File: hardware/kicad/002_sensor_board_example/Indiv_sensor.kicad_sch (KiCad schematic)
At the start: 5 parts, among them Q301 AO3400A, U301 VCNT2025X01

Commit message: Main Controller Board (1D) now added. Cheaper design, with RP2354, and BUCK PMIC
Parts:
- renumbered Q301 to Q4301, R301 to R4301, R302 to R4302, R303 to R4303, U301 to U4301
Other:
- company: (none) -> Noah Jaffe

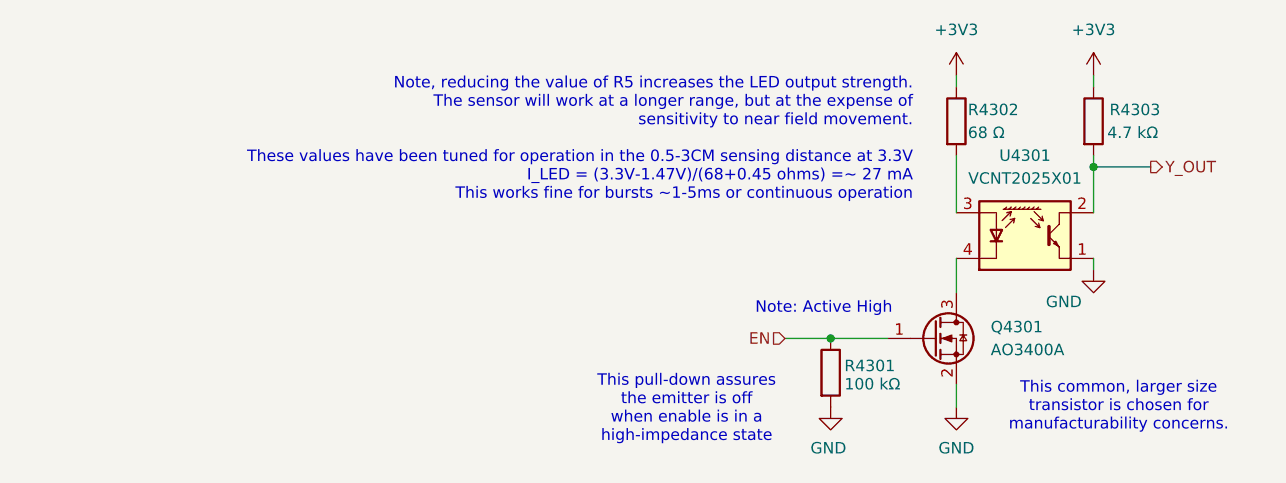
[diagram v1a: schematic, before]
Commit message: 001d bumped to 5V RS485 bus voltage. Sensor board schematic cleaned up, layout not begun
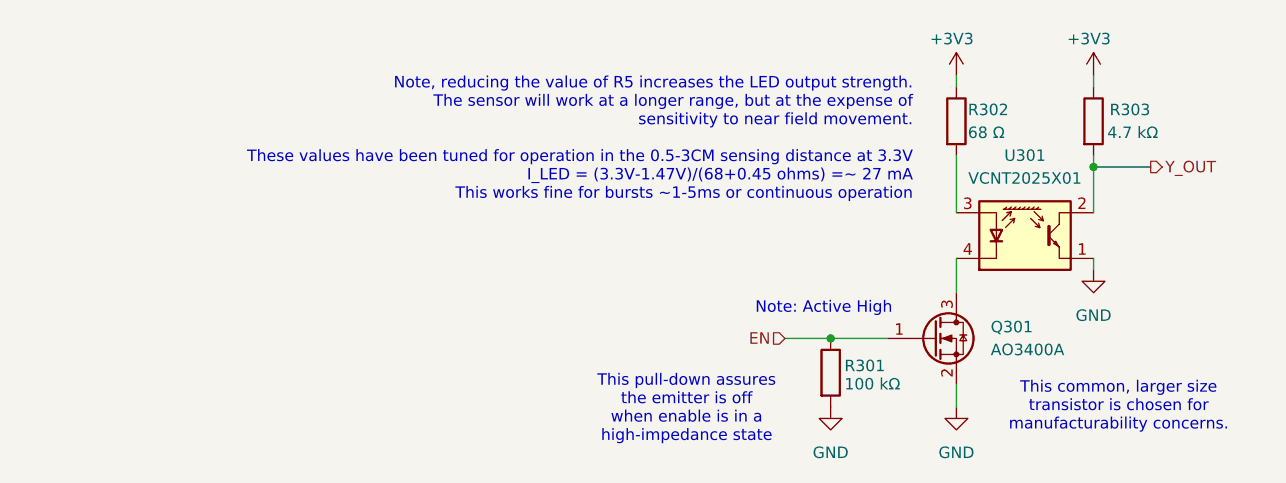
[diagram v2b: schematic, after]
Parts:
- renumbered Q4301 to Q301, R4301 to R301, R4302 to R302, R4303 to R303, U4301 to U301
